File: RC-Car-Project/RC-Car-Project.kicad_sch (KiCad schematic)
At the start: 0 parts

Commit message: XBEE + connector and mcu connector
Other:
- sheet Xbee ports: added UART_RX, UART_TX; removed none
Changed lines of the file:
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@@
 			)
 		)
-		(property "Value" "GND"
+		(property "Value" "GND_3V3"
 			(at 72.39 45.72 0)
 			(effects
@@
 			)
 		)
+		(pin "UART_TX" input
+			(at 77.47 90.17 0)
+			(effects
+				(font
+					(size 1.27 1.27)
+				)
+				(justify right)
+			)
+		)
+		(pin "UART_RX" input
+			(at 77.47 92.71 0)
+			(effects
+				(font
+					(size 1.27 1.27)
+				)
+				(justify right)
+			)
+		)

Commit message: Power: add converters
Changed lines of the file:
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@@
 	(paper "A4")
-	(no_connect
-		(at 72.39 40.64)
-	)
 	(no_connect
 		(at 90.17 34.29)
 	)
 	(no_connect
-		(at 90.17 40.64)
+		(at 102.87 34.29)
+	)
+	(no_connect
+		(at 102.87 40.64)
 	)
 	(no_connect
 		(at 72.39 34.29)
+	)
+	(wire
+		(pts
+			(xy 72.39 40.64) (xy 90.17 40.64)
+		)
+		(stroke
+			(width 0)
+			(type default)
+		)
 	)
 	(rectangle
@@
 			)
 		)
+	)
+	(symbol
+		(lib_id "power:+3V3")
+		(at 102.87 34.29 0)
+		(unit 1)
+		(exclude_from_sim no)
+		(in_bom yes)
+		(on_board yes)
+		(dnp no)
+		(fields_autoplaced yes)
+		(property "Reference" "#PWR017"
+			(at 102.87 38.1 0)
+			(effects
+				(font
+					(size 1.27 1.27)
+				)
+				(hide yes)
+			)
+		)
+		(property "Value" "5V_BUCK"
+			(at 102.87 29.21 0)
+			(effects
+				(font
+					(size 1.27 1.27)
+				)
+			)
+		)
+		(property "Footprint" ""
+			(at 102.87 34.29 0)
+			(effects
+				(font
+					(size 1.27 1.27)
+				)
+				(hide yes)
+			)
+		)
+		(property "Datasheet" ""
+			(at 102.87 34.29 0)
+			(effects
+				(font
+					(size 1.27 1.27)
+				)
+				(hide yes)
+			)
+		)
+		(property "Description" "Power symbol creates a global label with name \"+3V3\""
+			(at 102.87 34.29 0)
+			(effects
+				(font
+					(size 1.27 1.27)
+				)
+				(hide yes)
+			)
+		)
+		(pin "1"
+		)
+		(instances
+			(project "RC-Car-Project"
+				(path "/ba870fd1-751d-4755-8e1a-1ea86ca9e2f6"
+					(reference "#PWR017")
+					(unit 1)
+				)
+			)
+		)
+	)
+	(symbol
+		(lib_id "power:GND")
+		(at 102.87 40.64 0)
+		(unit 1)
+		(exclude_from_sim no)
+		(in_bom yes)
+		(on_board yes)
+		(dnp no)
+		(fields_autoplaced yes)
+		(property "Reference" "#PWR016"
+			(at 102.87 46.99 0)
+			(effects
+				(font
+					(size 1.27 1.27)
+				)
+				(hide yes)
+			)
+		)
+		(property "Value" "GND_BATT"
+			(at 102.87 45.72 0)
+			(effects
+				(font
+					(size 1.27 1.27)
+				)
+			)
+		)
+		(property "Footprint" ""
+			(at 102.87 40.64 0)
+			(effects
+				(font
+					(size 1.27 1.27)
+				)
+				(hide yes)
+			)
+		)
+		(property "Datasheet" ""
+			(at 102.87 40.64 0)
+			(effects
+				(font
+					(size 1.27 1.27)
+				)
+				(hide yes)
+			)
+		)
+		(property "Description" "Power symbol creates a global label with name \"GND\" , ground"
+			(at 102.87 40.64 0)
+			(effects
+				(font
+					(size 1.27 1.27)
+				)
+				(hide yes)
+			)
+		)
+		(pin "1"
+		)
+		(instances
+			(project "RC-Car-Project"
+				(path "/ba870fd1-751d-4755-8e1a-1ea86ca9e2f6"
+					(reference "#PWR016")
+					(unit 1)
+				)
+			)
+		)

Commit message: Add libraries and components in schs
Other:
- sheet Xbee renamed RF
- sheet RF: file Xbee_sch.kicad_sch -> RF_sch.kicad_sch
- sheet RF ports: added none; removed UART_RX, UART_TX
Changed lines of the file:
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@@
 			(color 0 0 0 0.0000)
 		)
-		(property "Sheetname" "Xbee"
+		(property "Sheetname" "RF"
 			(at 44.45 70.4084 0)
 			(effects
@@
 			)
 		)
-		(property "Sheetfile" "Xbee_sch.kicad_sch"
+		(property "Sheetfile" "RF_sch.kicad_sch"
 			(at 44.45 98.3746 0)
 			(effects
@@
 			)
 		)
-		(pin "UART_TX" input
-			(at 77.47 90.17 0)
-			(effects
-				(font
-					(size 1.27 1.27)
-				)
-				(justify right)
-			)
-		)
-		(pin "UART_RX" input
-			(at 77.47 92.71 0)
-			(effects
-				(font
-					(size 1.27 1.27)
-				)
-				(justify right)
-			)
-		)

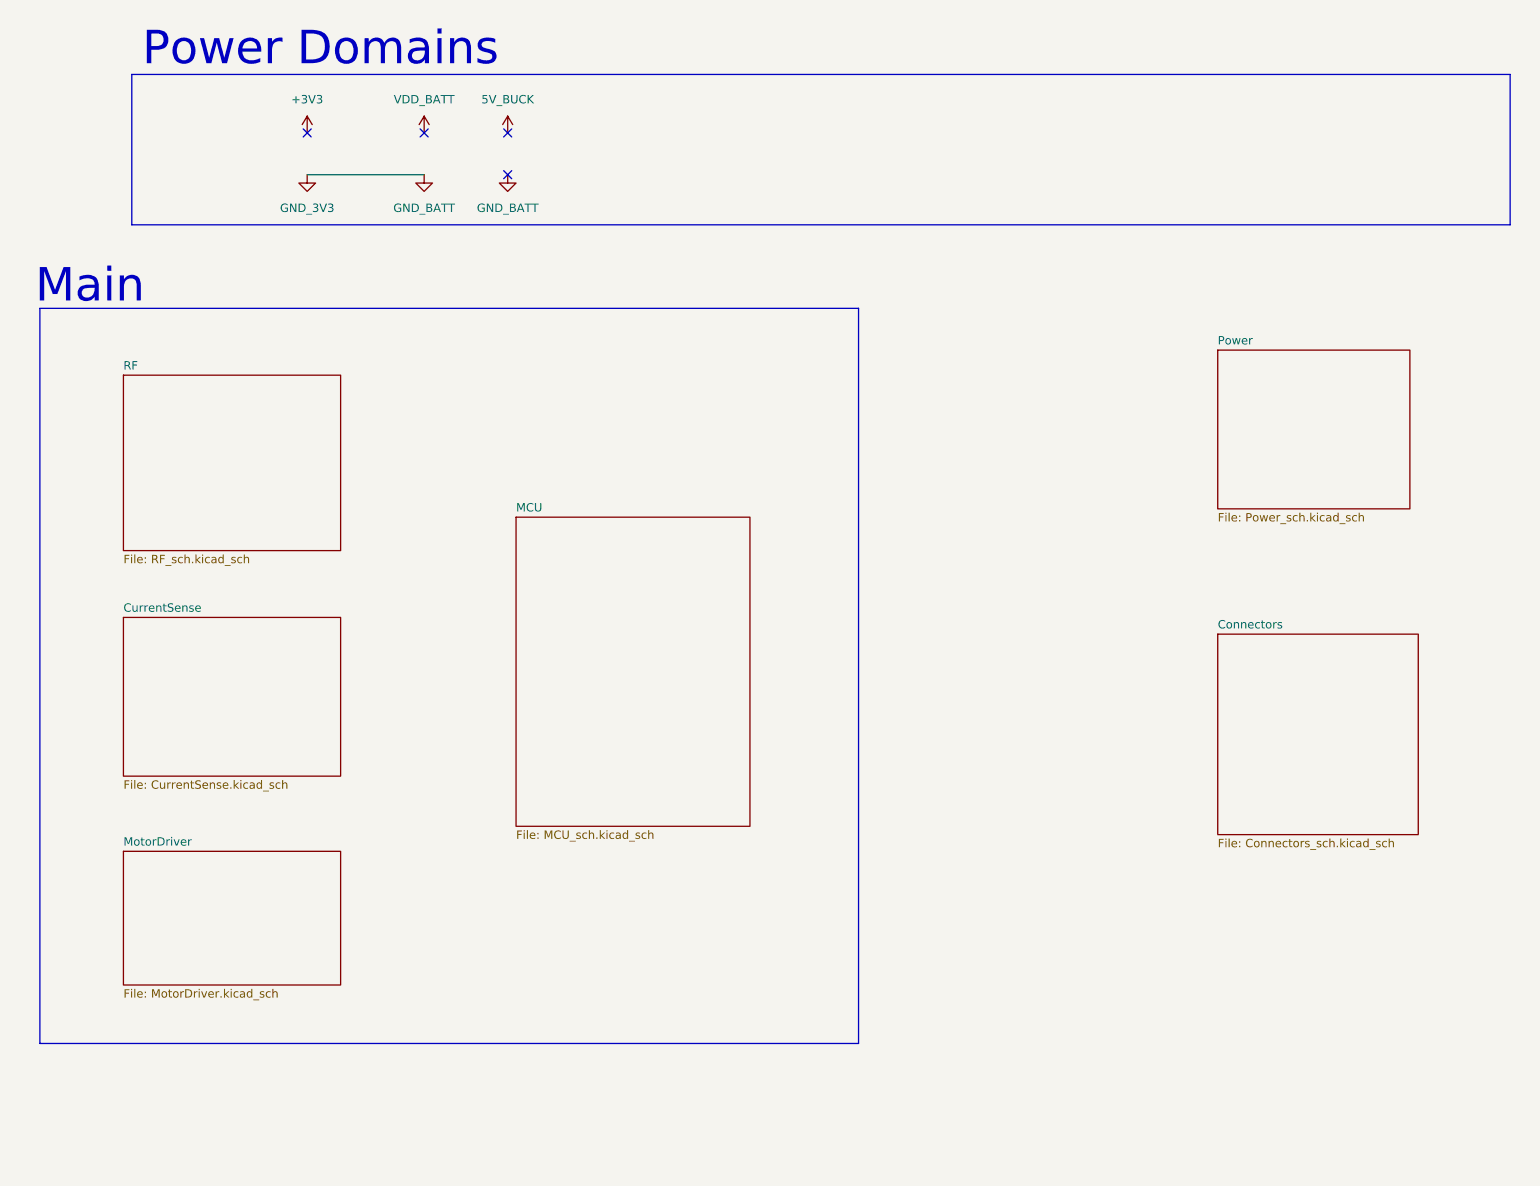
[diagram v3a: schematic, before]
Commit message: Added Basic Schematic + STM32 Project config. TODO: Component value selection + double check all connections.
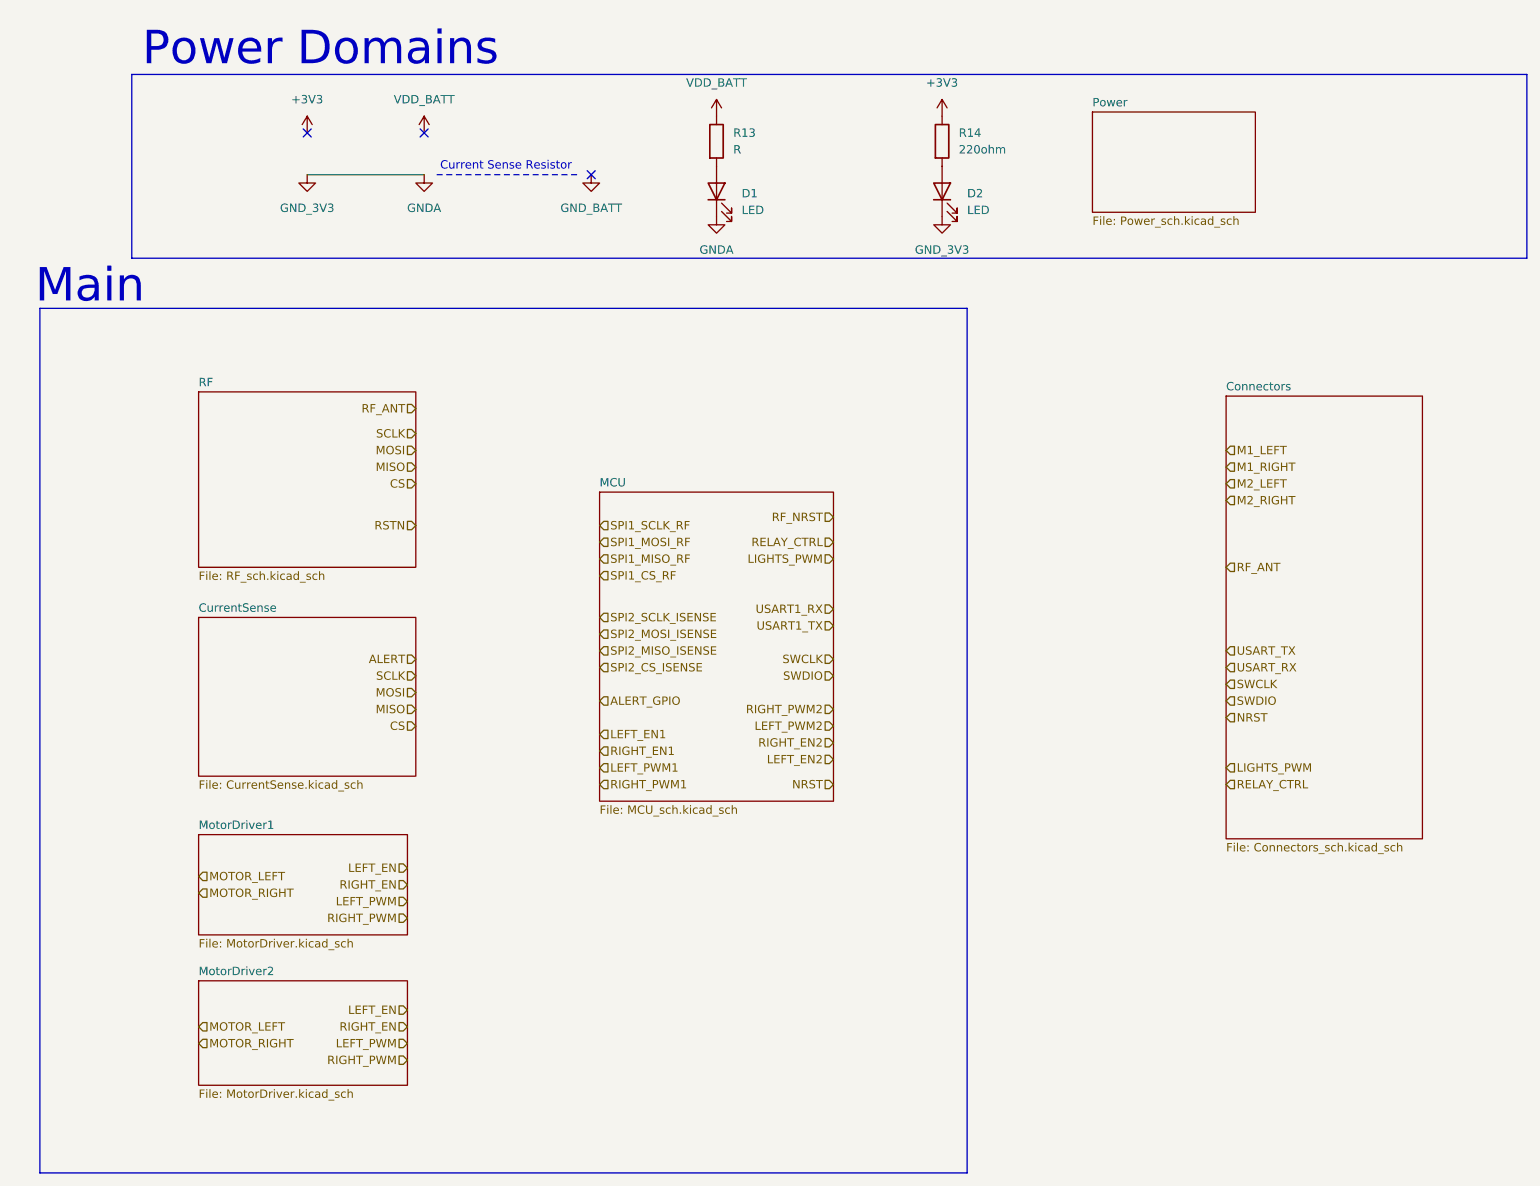
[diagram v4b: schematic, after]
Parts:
- added D1, D2: LED, symbol Device:LED
- added R13: R, symbol Device:R
- added R14: 220ohm, symbol Device:R
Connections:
- net +3V3: now also R14.1
- net VDD_BATT: now also R13.1
- new net: D1.2 (A), R13.2
- new net: D2.2 (A), R14.2
- new net GNDA: D1.1 (K), D2.1 (K)
- no-connect marks 4 -> 3
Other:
- sheet MotorDriver renamed MotorDriver1
- added sheet MotorDriver2 (MotorDriver.kicad_sch)
- note added: "Current Sense Resistor"

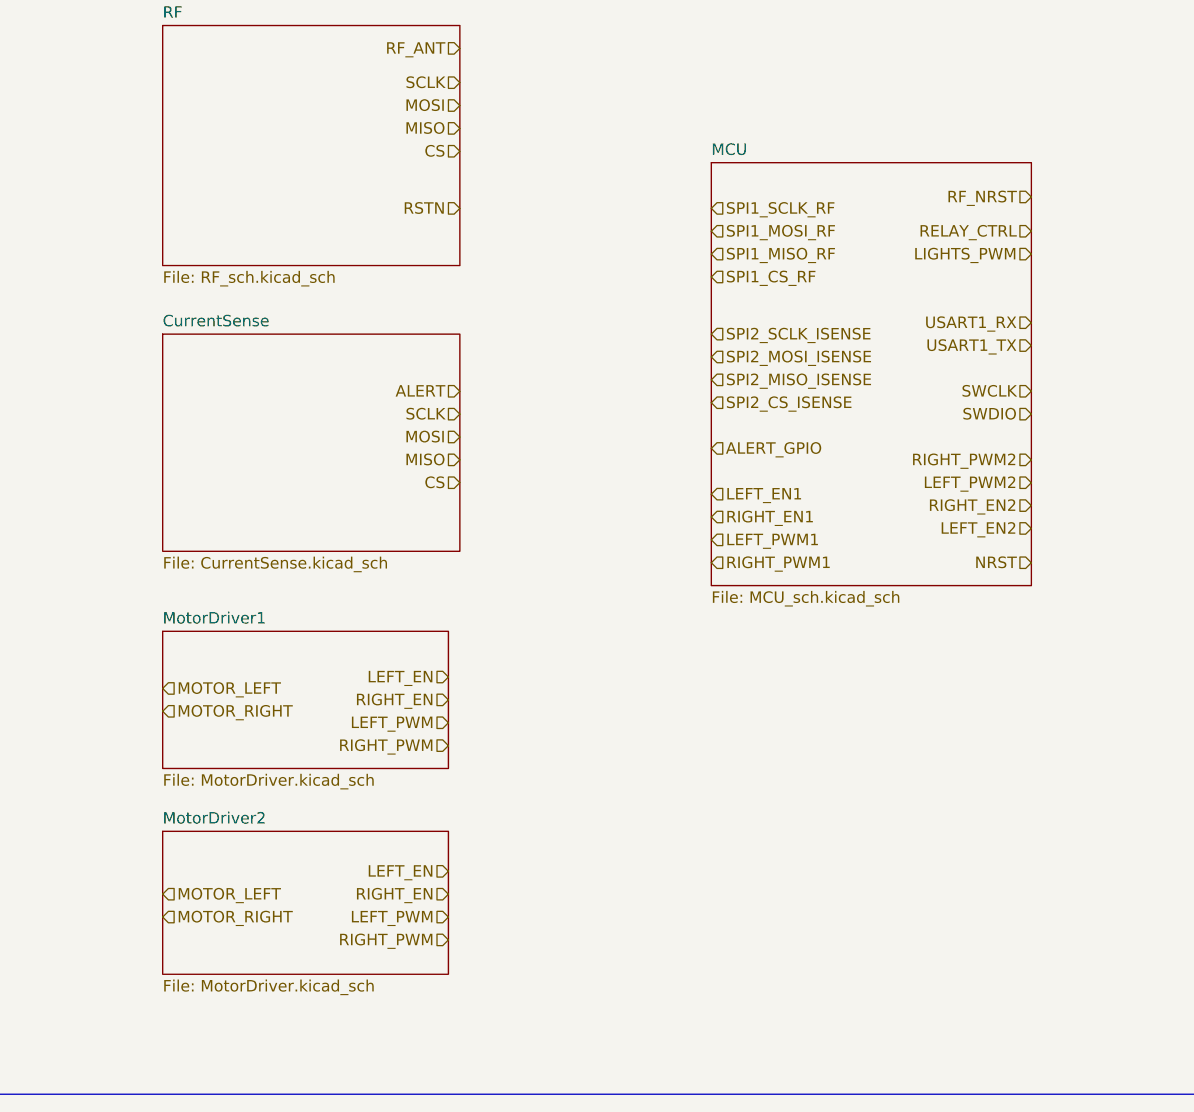
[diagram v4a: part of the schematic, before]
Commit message: Cleaned up Motor Circuit
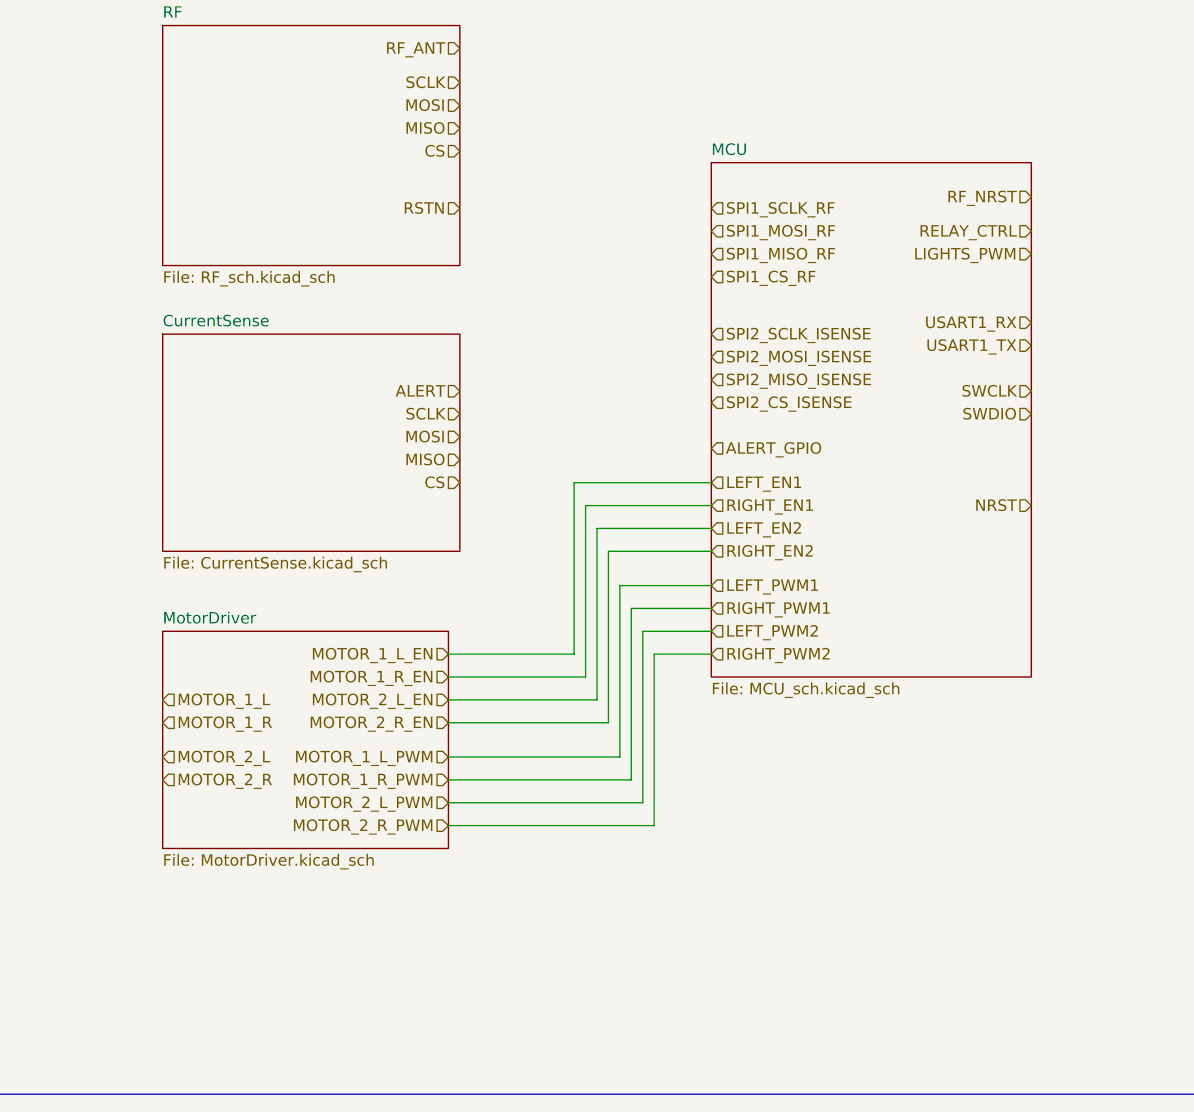
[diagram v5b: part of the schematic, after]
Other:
- sheet MotorDriver1 renamed MotorDriver
- removed sheet MotorDriver2
